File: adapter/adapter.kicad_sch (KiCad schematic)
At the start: 23 parts, among them J1 Serial, J10 Ribbon, J3 Battery charge, J4 RGB, J9 Ribbon, SW1 SW_SPST, SW3 SW_SPDT, U1 Dual MCU: RP2040 + nice!nano, U6 AP1603WG-7

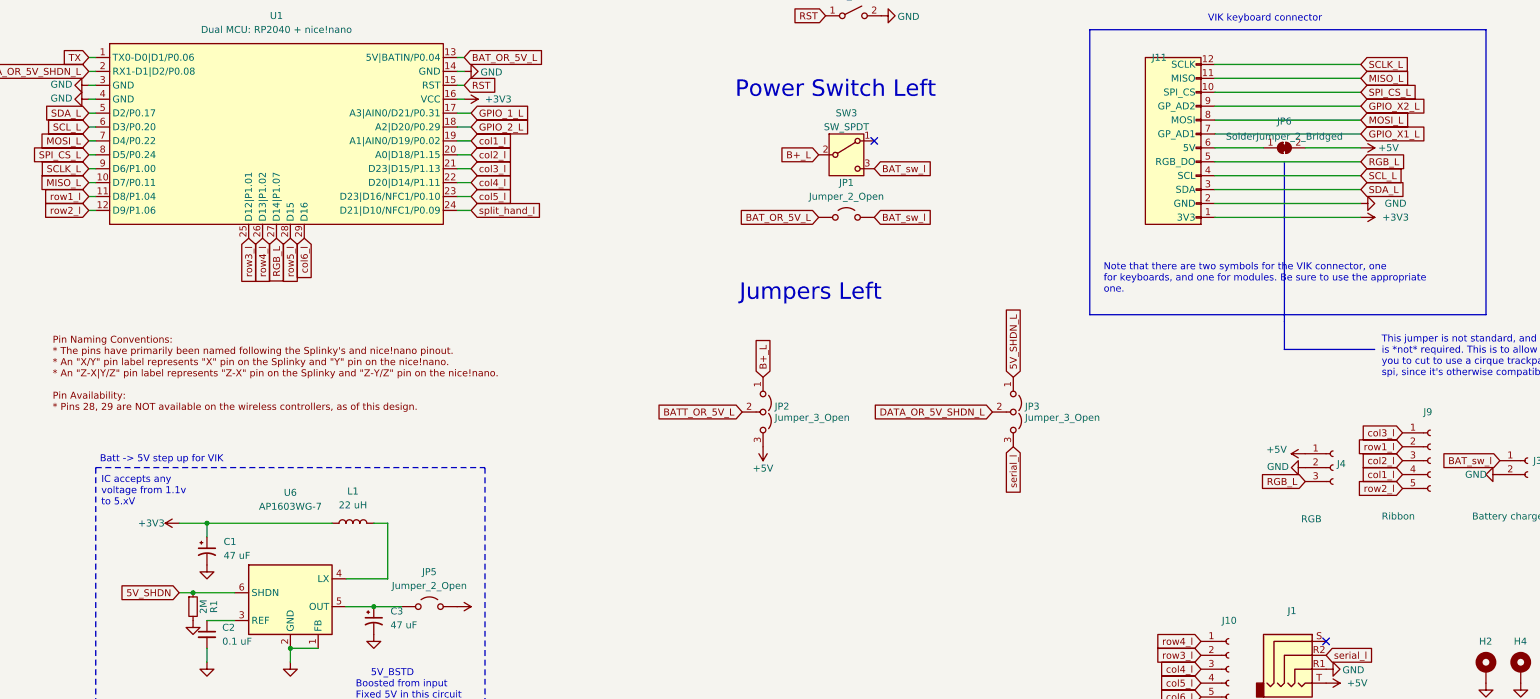
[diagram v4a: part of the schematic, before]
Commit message: sch: fix up erc violations and issues
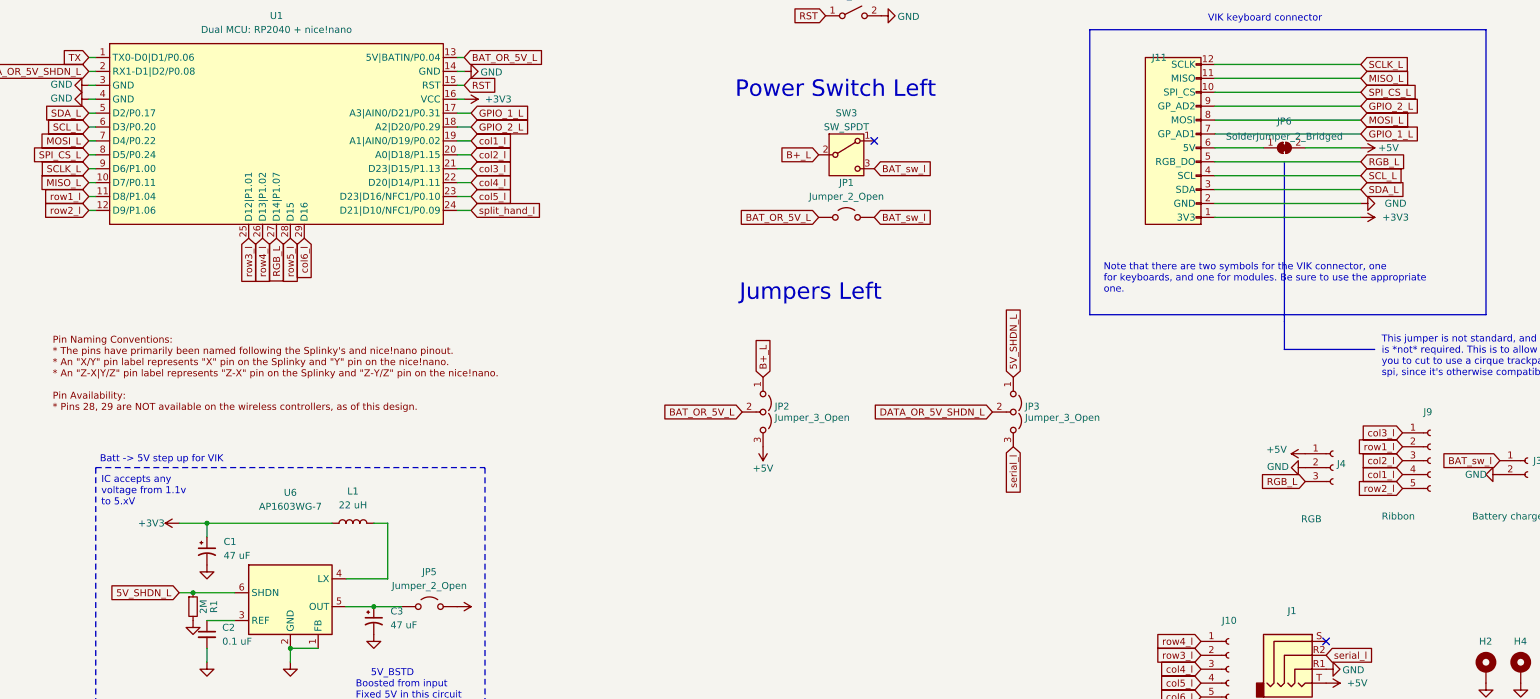
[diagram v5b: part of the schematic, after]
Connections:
- net 5V_SHDN is gone; now on net 5V_SHDN_L: R1.1, U6.6 (SHDN)
- net BATT_OR_5V_L is gone; now on net BAT_OR_5V_L: JP2.2 (C)
- net GPIO_X1_L is gone; now on net GPIO_1_L: J11.7 (GP_AD1)
- net GPIO_X2_L is gone; now on net GPIO_2_L: J11.9 (GP_AD2)
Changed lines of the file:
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@@
 		)
 	)
-	(global_label "GPIO_X1_L"
+	(global_label "GPIO_1_L"
 		(shape input)
 		(at 261.62 60.96 0)
@@
 		)
 		(property "Intersheetrefs" "${INTERSHEET_REFS}"
-			(at 274.5579 60.96 0)
+			(at 273.3484 60.96 0)
 			(effects
 				(font
@@
 		)
 	)
-	(global_label "BATT_OR_5V_L"
+	(global_label "BAT_OR_5V_L"
 		(shape input)
 		(at 148.59 111.76 180)
@@
 		)
 		(property "Intersheetrefs" "${INTERSHEET_REFS}"
-			(at 132.3864 111.76 0)
+			(at 133.354 111.76 0)
 			(effects
 				(font
@@
 		)
 	)
-	(global_label "GPIO_X2_L"
+	(global_label "GPIO_2_L"
 		(shape input)
 		(at 261.62 55.88 0)
@@
 		)
 		(property "Intersheetrefs" "${INTERSHEET_REFS}"
-			(at 274.5579 55.88 0)
+			(at 273.3484 55.88 0)
 			(effects
 				(font
@@
 		)
 	)
-	(global_label "5V_SHDN"
+	(global_label "5V_SHDN_L"
 		(shape input)
 		(at 45.72 144.78 180)
@@
 		)
 		(property "Intersheetrefs" "${INTERSHEET_REFS}"
-			(at 34.3129 144.78 0)
+			(at 32.2378 144.78 0)
 			(effects
 				(font
@@
 	)
 	(symbol
+		(lib_name "+3V3_1")
 		(lib_id "power:+3V3")
 		(at 45.72 132.08 90)
@@
 			)
 		)
-		(property "Description" ""
+		(property "Description" "Power symbol creates a global label with name \"+3V3\""
 			(at 45.72 132.08 0)
 			(effects
@@
 			)
 		)
-		(property "Description" ""
+		(property "Description" "Power symbol creates a global label with name \"+3V3\""
 			(at 261.62 76.2 0)
 			(effects

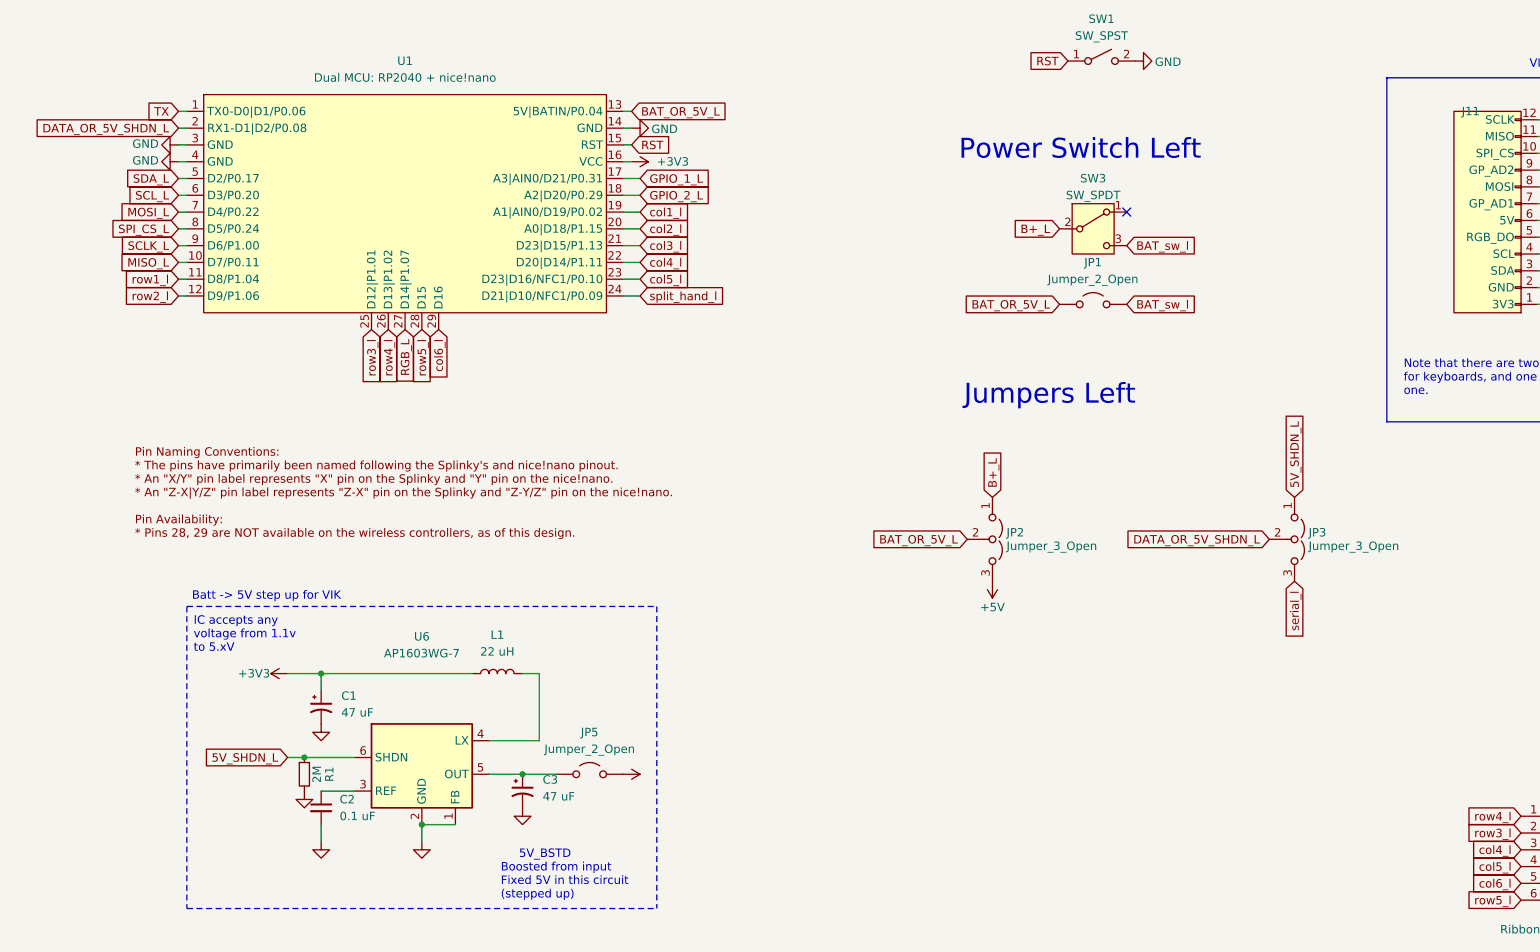
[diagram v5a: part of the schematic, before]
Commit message: always have voltage convertor on
Signed-off-by: Anant Thazhemadam <anant.thazhemadam@gmail.com>
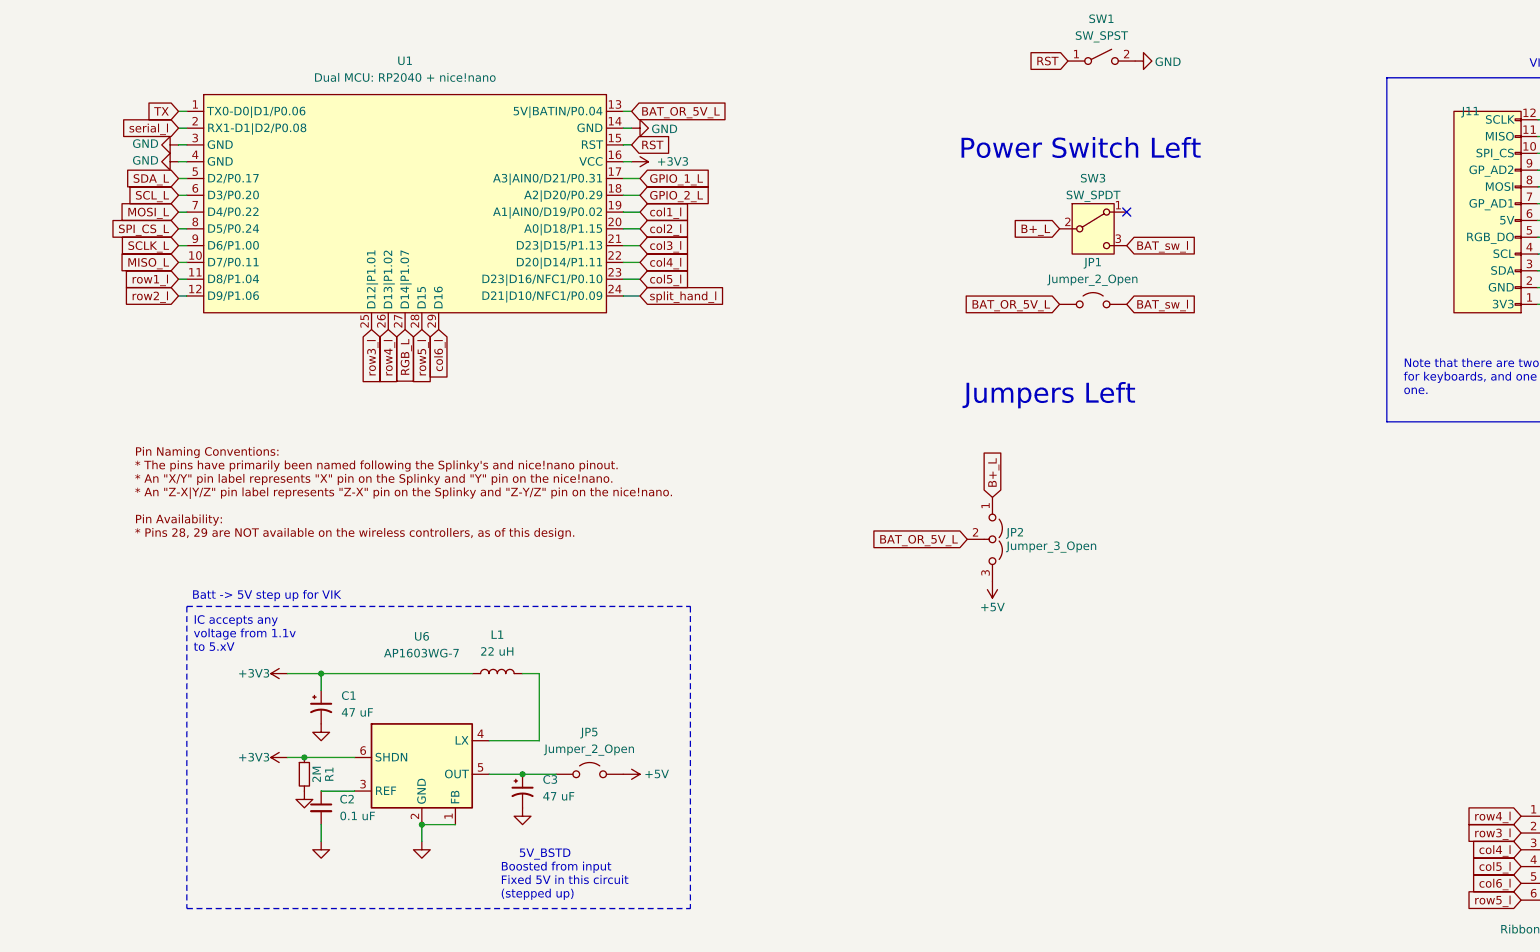
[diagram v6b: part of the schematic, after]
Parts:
- removed JP3: Jumper_3_Open, Jumper:SolderJumper-3_P1.3mm_Open_RoundedPad1.0x1.5mm, symbol Jumper:Jumper_3_Open
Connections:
- net 5V_SHDN_L is gone; now on net +3V3: R1.1, U6.6 (SHDN)
- net DATA_OR_5V_SHDN_L is gone; now on net serial_l: U1.2 (RX1-D1|D2/P0.08)
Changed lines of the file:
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@@
 	(polyline
 		(pts
-			(xy 30.48 167.64) (xy 101.6 167.64)
+			(xy 30.48 167.64) (xy 106.68 167.64)
 		)
 		(stroke
@@
 	(polyline
 		(pts
-			(xy 30.48 121.92) (xy 101.6 121.92)
+			(xy 30.48 121.92) (xy 106.68 121.92)
 		)
 		(stroke
@@
 	(polyline
 		(pts
-			(xy 101.6 121.92) (xy 101.6 167.64)
+			(xy 106.68 121.92) (xy 106.68 167.64)
 		)
 		(stroke
@@
 		)
 	)
+	(global_label "serial_l"
+		(shape input)
+		(at 29.21 49.53 180)
+		(effects
+			(font
+				(size 1.27 1.27)
+			)
+			(justify right)
+		)
+		(property "Intersheetrefs" "${INTERSHEET_REFS}"
+			(at 21.475 49.4506 0)
+			(effects
+				(font
+					(size 1.27 1.27)
+				)
+				(justify right)
+				(hide yes)
+			)
+		)
+	)
 	(global_label "GPIO_1_L"
 		(shape input)
@@
 		)
 	)
-	(global_label "5V_SHDN_L"
-		(shape input)
-		(at 198.12 105.41 90)
-		(fields_autoplaced yes)
-		(effects
-			(font
-				(size 1.27 1.27)
-			)
-			(justify left)
-		)
-		(property "Intersheetrefs" "${INTERSHEET_REFS}"
-			(at 198.12 91.9278 90)
-			(effects
-				(font
-					(size 1.27 1.27)
-				)
-				(justify left)
-				(hide yes)
-			)
-		)
-	)
 	(global_label "BAT_OR_5V_L"
 		(shape input)
@@
 		)
 	)
-	(global_label "serial_l"
-		(shape input)
-		(at 198.12 118.11 270)
-		(effects
-			(font
-				(size 1.27 1.27)
-			)
-			(justify right)
-		)
-		(property "Intersheetrefs" "${INTERSHEET_REFS}"
-			(at 198.0406 125.845 90)
-			(effects
-				(font
-					(size 1.27 1.27)
-				)
-				(justify right)
-				(hide yes)
-			)
-		)
-	)
 	(global_label "row4_l"
 		(shape input)
@@
 		)
 	)
-	(global_label "DATA_OR_5V_SHDN_L"
-		(shape input)
-		(at 29.21 49.53 180)
-		(fields_autoplaced yes)
-		(effects
-			(font
-				(size 1.27 1.27)
-			)
-			(justify right)
-		)
-		(property "Intersheetrefs" "${INTERSHEET_REFS}"
-			(at 6.7773 49.53 0)
-			(effects
-				(font
-					(size 1.27 1.27)
-				)
-				(justify right)
-				(hide yes)
-			)
-		)
-	)
 	(global_label "row3_l"
 		(shape input)
@@
 		)
 	)
-	(global_label "DATA_OR_5V_SHDN_L"
-		(shape input)
-		(at 194.31 111.76 180)
-		(fields_autoplaced yes)
-		(effects
-			(font
-				(size 1.27 1.27)
-			)
-			(justify right)
-		)
-		(property "Intersheetrefs" "${INTERSHEET_REFS}"
-			(at 171.8773 111.76 0)
-			(effects
-				(font
-					(size 1.27 1.27)
-				)
-				(justify right)
-				(hide yes)
-			)
-		)
-	)
 	(global_label "row4_l"
 		(shape input)
@@
 		)
 	)
-	(global_label "5V_SHDN_L"
-		(shape input)
-		(at 45.72 144.78 180)
-		(fields_autoplaced yes)
-		(effects
-			(font
-				(size 1.27 1.27)
-			)
-			(justify right)
-		)
-		(property "Intersheetrefs" "${INTERSHEET_REFS}"
-			(at 32.2378 144.78 0)
-			(effects
-				(font
-					(size 1.27 1.27)
-				)
-				(justify right)
-				(hide yes)
-			)
-		)
-	)
 	(global_label "BAT_sw_l"
 		(shape input)
@@
 	)
 	(symbol
+		(lib_name "+3V3_1")
+		(lib_id "power:+3V3")
+		(at 45.72 144.78 90)
+		(unit 1)
+		(exclude_from_sim no)
+		(in_bom yes)
+		(on_board yes)
+		(dnp no)
+		(property "Reference" "#PWR05"
+			(at 49.53 144.78 0)
+			(effects
+				(font
+					(size 1.27 1.27)
+				)
+				(hide yes)
+			)
+		)
+		(property "Value" "+3V3"
+			(at 40.64 144.78 90)
+			(effects
+				(font
+					(size 1.27 1.27)
+				)
+			)
+		)
+		(property "Footprint" ""
+			(at 45.72 144.78 0)
+			(effects
+				(font
+					(size 1.27 1.27)
+				)
+				(hide yes)
+			)
+		)
+		(property "Datasheet" ""
+			(at 45.72 144.78 0)
+			(effects
+				(font
+					(size 1.27 1.27)
+				)
+				(hide yes)
+			)
+		)
+		(property "Description" "Power symbol creates a global label with name \"+3V3\""
+			(at 45.72 144.78 0)
+			(effects
+				(font
+					(size 1.27 1.27)
+				)
+				(hide yes)
+			)
+		)
+		(pin "1"
+		)
+		(instances
+			(project "adapter"
+				(path "/e63e39d7-6ac0-4ffd-8aa3-1841a4541b55"
+					(reference "#PWR05")
+					(unit 1)
+				)
+			)
+		)
+	)
+	(symbol
 		(lib_id "power:+5V")
 		(at 251.46 119.38 90)
@@
 	)
 	(symbol
-		(lib_id "power:+5V")
-		(at 96.52 147.32 270)
-		(unit 1)
-		(exclude_from_sim no)
-		(in_bom yes)
-		(on_board yes)
-		(dnp no)
-		(fields_autoplaced yes)
-		(property "Reference" "#PWR033"
-			(at 92.71 147.32 0)
-			(effects
-				(font
-					(size 1.27 1.27)
-				)
-				(hide yes)
-			)
-		)
-		(property "Value" "+5V"
-			(at 99.695 147.32 90)
-			(effects
-				(font
-					(size 1.27 1.27)
-				)
-				(justify left)
-				(hide yes)
-			)
-		)
-		(property "Footprint" ""
-			(at 96.52 147.32 0)
-			(effects
-				(font
-					(size 1.27 1.27)
-				)
-				(hide yes)
-			)
-		)
-		(property "Datasheet" ""
-			(at 96.52 147.32 0)
-			(effects
-				(font
-					(size 1.27 1.27)
-				)
-				(hide yes)
-			)
-		)
-		(property "Description" ""
-			(at 96.52 147.32 0)
-			(effects
-				(font
-					(size 1.27 1.27)
-				)
-				(hide yes)
-			)
-		)
-		(pin "1"
-		)
-		(instances
-			(project "adapter"
-				(path "/e63e39d7-6ac0-4ffd-8aa3-1841a4541b55"
-					(reference "#PWR033")
-					(unit 1)
-				)
-			)
-		)
-	)
-	(symbol
 		(lib_id "power:GND")
 		(at 29.21 52.07 270)
@@
 	(symbol
 		(lib_id "power:+5V")
+		(at 96.52 147.32 270)
+		(unit 1)
+		(exclude_from_sim no)
+		(in_bom yes)
+		(on_board yes)
+		(dnp no)
+		(property "Reference" "#PWR06"
+			(at 92.71 147.32 0)
+			(effects
+				(font
+					(size 1.27 1.27)
+				)
+				(hide yes)
+			)
+		)
+		(property "Value" "+5V"
+			(at 99.695 147.32 90)
+			(effects
+				(font
+					(size 1.27 1.27)
+				)
+				(justify left)
+			)
+		)
+		(property "Footprint" ""
+			(at 96.52 147.32 0)
+			(effects
+				(font
+					(size 1.27 1.27)
+				)
+				(hide yes)
+			)
+		)
+		(property "Datasheet" ""
+			(at 96.52 147.32 0)
+			(effects
+				(font
+					(size 1.27 1.27)
+				)
+				(hide yes)
+			)
+		)
+		(property "Description" ""
+			(at 96.52 147.32 0)
+			(effects
+				(font
+					(size 1.27 1.27)
+				)
+				(hide yes)
+			)
+		)
+		(pin "1"
+		)
+		(instances
+			(project "adapter"
+				(path "/e63e39d7-6ac0-4ffd-8aa3-1841a4541b55"
+					(reference "#PWR06")
+					(unit 1)
+				)
+			)
+		)
+	)
+	(symbol
+		(lib_id "power:+5V")
 		(at 97.79 54.61 270)
 		(unit 1)
@@
 					(unit 1)
 				)
-			)
-		)
-	)
-	(symbol
-		(lib_id "Jumper:Jumper_3_Open")
-		(at 198.12 111.76 270)
-		(unit 1)
-		(exclude_from_sim no)
-		(in_bom yes)
-		(on_board yes)
-		(dnp no)
-		(fields_autoplaced yes)
-		(property "Reference" "JP3"
-			(at 200.2542 110.736 90)
-			(effects
-				(font
-					(size 1.27 1.27)
-				)
-				(justify left)
-			)
-		)
-		(property "Value" "Jumper_3_Open"
-			(at 200.2542 112.784 90)
-			(effects
-				(font
-					(size 1.27 1.27)
-				)
-				(justify left)
-			)
-		)
-		(property "Footprint" "Jumper:SolderJumper-3_P1.3mm_Open_RoundedPad1.0x1.5mm"
-			(at 198.12 111.76 0)
-			(effects
-				(font
-					(size 1.27 1.27)
-				)
-				(hide yes)
-			)
-		)
-		(property "Datasheet" "~"
-			(at 198.12 111.76 0)
-			(effects
-				(font
-					(size 1.27 1.27)
-				)
-				(hide yes)
-			)
-		)
-		(property "Description" ""
-			(at 198.12 111.76 0)
-			(effects
-				(font
-					(size 1.27 1.27)
-				)
-				(hide yes)
-			)
-		)
-		(pin "1"
-		)
-		(pin "2"
-		)
-		(pin "3"
-		)
-		(instances
-			(project "adapter"
-				(path "/e63e39d7-6ac0-4ffd-8aa3-1841a4541b55"
-					(reference "JP3")
-					(unit 1)
-				)

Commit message: sch: organize different things
Signed-off-by: Anant Thazhemadam <anant.thazhemadam@gmail.com>
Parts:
- removed JP5: Jumper_2_Open, Jumper:SolderJumper-2_P1.3mm_Open_RoundedPad1.0x1.5mm, symbol Jumper:Jumper_2_Open
- removed U6: AP1603WG-7, Package_TO_SOT_SMD:SOT-23-6, symbol AP1603WG-7:AP1603WG-7
- added JP3: Jumper_2_Open, Jumper:SolderJumper-2_P1.3mm_Open_RoundedPad1.0x1.5mm, symbol Jumper:Jumper_2_Open
- added U2: AP1603WG-7, Package_TO_SOT_SMD:SOT-23-6, symbol AP1603WG-7:AP1603WG-7
- C1, C3: footprint Capacitor_SMD:C_0603_1608Metric -> Capacitor_SMD:C_0805_2012Metric_Pad1.18x1.45mm_HandSolder
- C2: footprint Capacitor_SMD:C_0402_1005Metric -> Capacitor_SMD:C_0805_2012Metric_Pad1.18x1.45mm_HandSolder
- L1: footprint Inductor_SMD:L_0603_1608Metric -> Inductor_SMD:L_0805_2012Metric_Pad1.15x1.40mm_HandSolder
- R1: footprint Resistor_SMD:R_0402_1005Metric_Pad0.72x0.64mm_HandSolder -> Resistor_SMD:R_0805_2012Metric_Pad1.20x1.40mm_HandSolder
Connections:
- net +3V3: now also U2.6 (SHDN)
- net +5V: now also JP3.2 (B)
- net BAT_OR_5V_L: no longer JP2.2 (C)
- net GND: now also U2.1 (FB), U2.2 (GND)
- net at L1.2: now also U2.4 (LX)
- net at C2.1: now also U2.3 (REF)
- net at C3.1: now also JP3.1 (A), U2.5 (OUT)
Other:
- note added: "5V Booster Circuit for VIK Left"
- note added: "Handedness selection works by pulling a dedicated pin high or low. This is checked upon boot and the correct side is set at runtime. The default is high for the left side and low for the right side, but this can be overwritten in firmware."
- note added: "TRRS Left"
- note added: "V I K K E Y B O A R D C O N N E C T O R"
- note removed: "Handedness selection works by pulling a dedicated pin high or low this is checked upon boot and the correct side is set at runtime. The default is high for the left side and low for the right side, but this can be overwritten in firmware."
- note removed: "Note that there are two symbols for the VIK connector, one for keyboards, and one for modules. Be sure to use the appropriate one."
- note removed: "VIK keyboard connector"
- moved on the sheet: H2, H4, J1, J10, J11, J3, J4, J9, JP1, JP2, SW1, SW3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
